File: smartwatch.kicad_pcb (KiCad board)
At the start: 4 copper layers, 38 x 38 mm, 52 parts, among them IC1 W25N01GVZEIG, IC2 NORA-B120-00B, J1 Charging_Pad-, J2 Charging_Pad+, J3 DS1020-09-15VBT1A, J4 Conn_01x04_Pin, Q1 2N7002, Q2 AO3401, Q6 AO3401, U1 MAX17048G+T10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

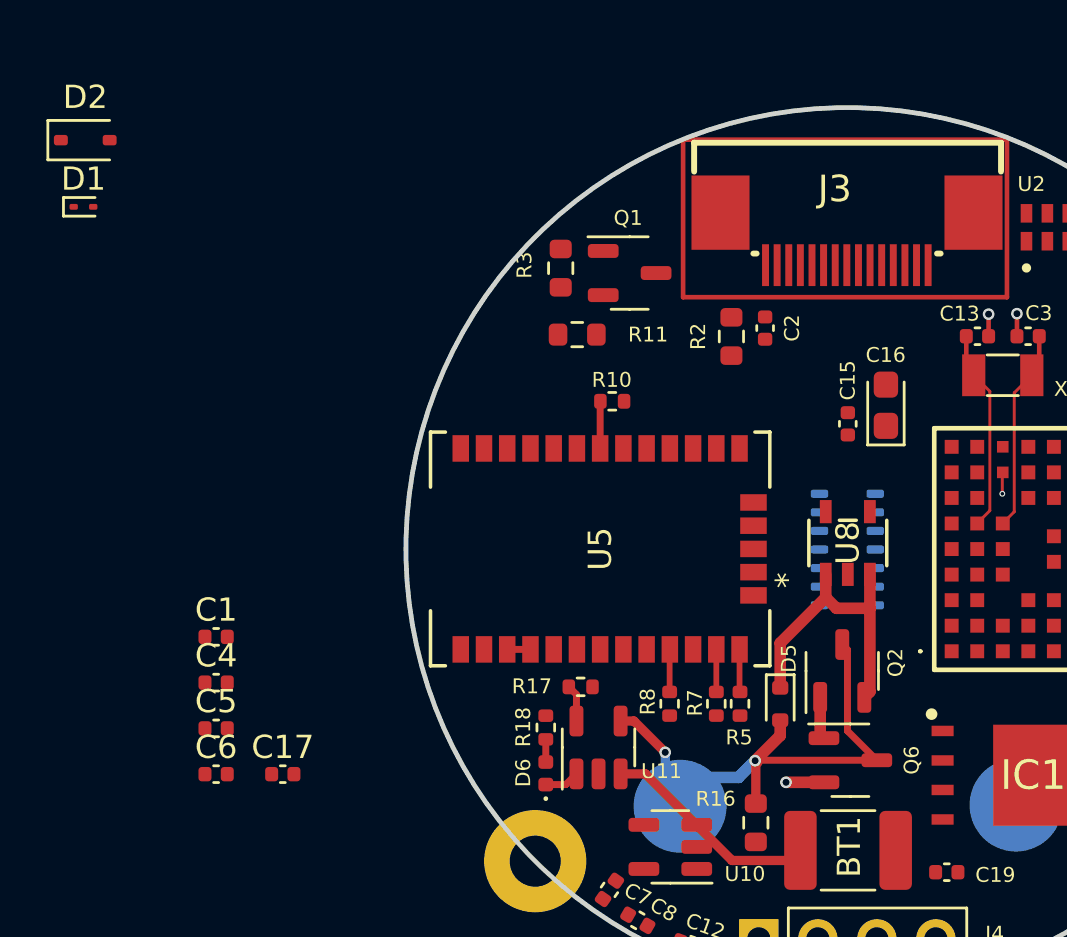
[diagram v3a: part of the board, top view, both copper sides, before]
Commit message: added lm66200
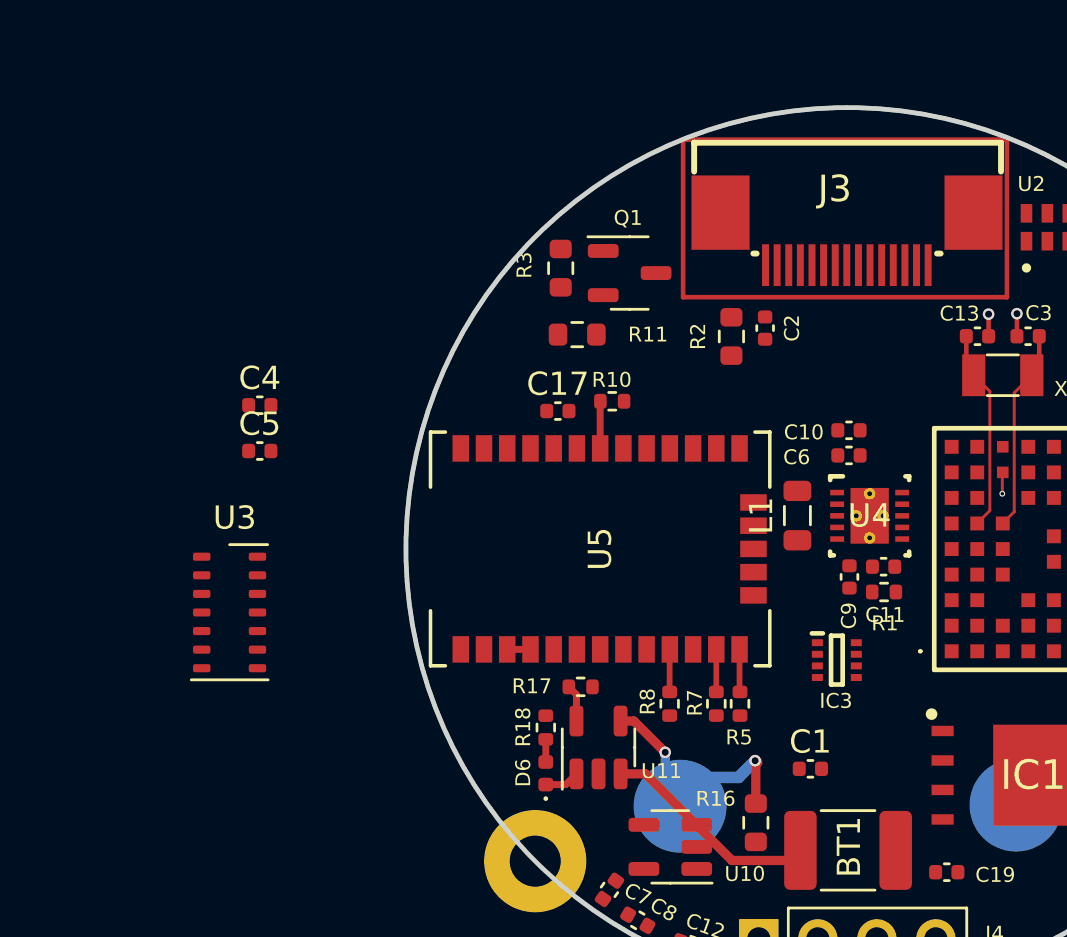
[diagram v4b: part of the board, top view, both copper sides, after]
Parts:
- removed C15: 100uF, Capacitor_SMD:C_0402_1005Metric
- removed C16: 4.7uF, Capacitor_Tantalum_SMD:CP_EIA-2012-12_Kemet-R
- removed D1: CDBQC0130L-HF, Diode_SMD:D_SOD-923
- removed D2: CUS08F30,H3F, Diode_SMD:D_SOD-323
- removed D5: LBAT54XV2T1G, Diode_SMD:D_SOD-523
- removed Q2, Q6: AO3401, Package_TO_SOT_SMD:SOT-23-3
- removed U8: AP2112K-3.3TRG1, AP2112K-3-3TRG1:SOT_RG1_DIO
- added C10: 10uF, Capacitor_SMD:C_0402_1005Metric, F.Cu at (152.6, 88.5)
- added C11: 0.1uF, Capacitor_SMD:C_0402_1005Metric, F.Cu at (154.1, 94.4)
- added C9: 10uF, Capacitor_SMD:C_0402_1005Metric, F.Cu at (152.6, 94.8)
- added IC3: LM66200DRLR, LM66200DRLR:SOTFL50P160X60-8N, F.Cu at (152.1, 98.4)
- added L1: MLZ2012M1R0HT000, Inductor_SMD:L_0805_2012Metric, F.Cu at (150.4, 92.2)
- added R1: 100, Resistor_SMD:R_0402_1005Metric, F.Cu at (154.1, 95.5)
- added U4: TPS63001DRCR, TPS63001DRCR:DRC0010J, F.Cu at (153.5, 92.2)
- C6: value 1uF -> 10uF
- U3: moved to F.Cu
- moved C6 30.5 mm to (152.6, 89.6)
- moved U3 26.7 mm to (125.9, 96.4), turned to 0 degrees
- moved C1 26.2 mm to (150.9, 103.1)
- moved C17 19.6 mm to (140.1, 87.7)
- moved C4 12.1 mm to (127.2, 87.5)
- moved C5 12.1 mm to (127.2, 89.4)
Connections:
- C1 pad 1: VBUS -> Net-(IC3-VIN1)
- C6 pad 1: Net-(D5-K) -> VSYS
- J2 pad 1: VBUS -> Net-(IC3-VIN1)
- R18 pad 1: VBUS -> Net-(IC3-VIN1)
- U10 pad 1: /BAT+ -> VBUS
- U10 pad 3: /BAT+ -> VBUS
- U11 pad 4: VBUS -> Net-(IC3-VIN1)
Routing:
- net Net-(D5-K): track 13.2 -> 0.00 mm
- net VBUS: track 24.1 -> 11.1 mm
- net Net-(Q2-D): track 1.82 -> 0.00 mm
- net /BAT+: track 11.6 -> 10.0 mm, vias 1 -> 0

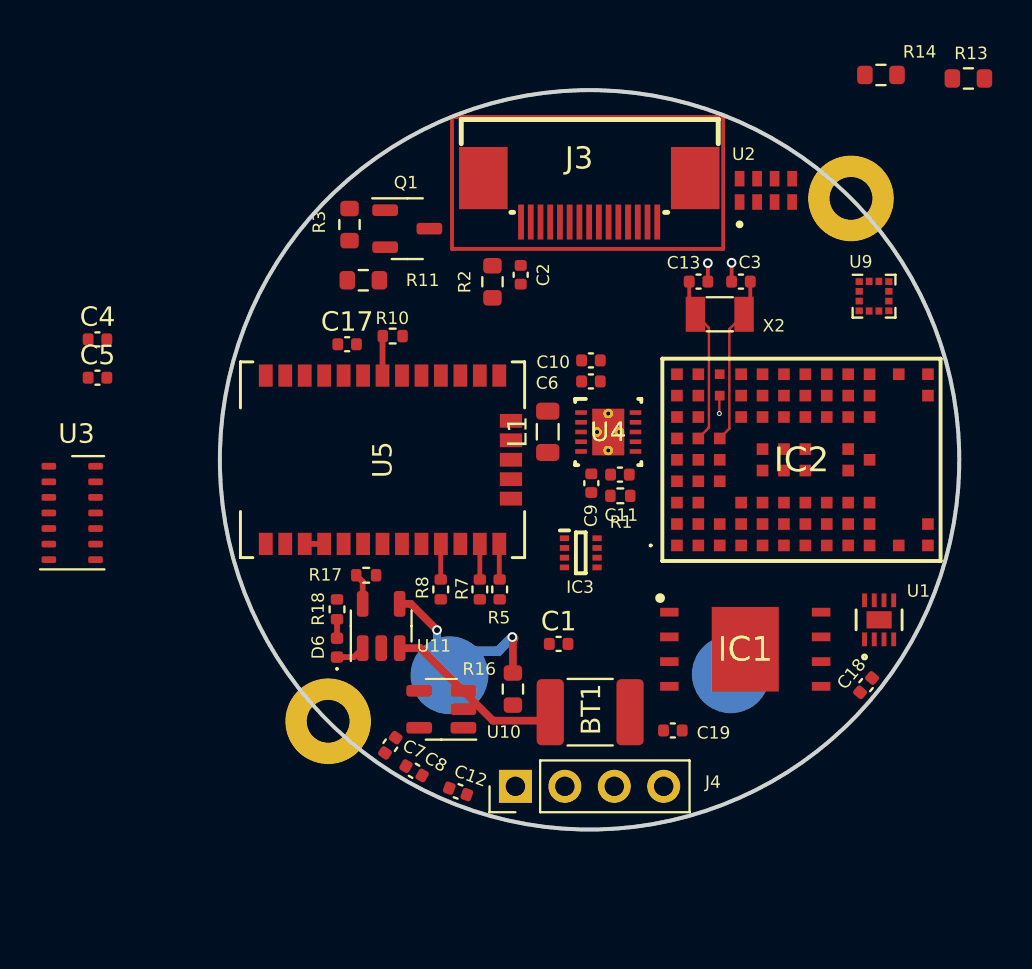
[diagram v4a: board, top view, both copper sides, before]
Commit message: signal routing 50% complete
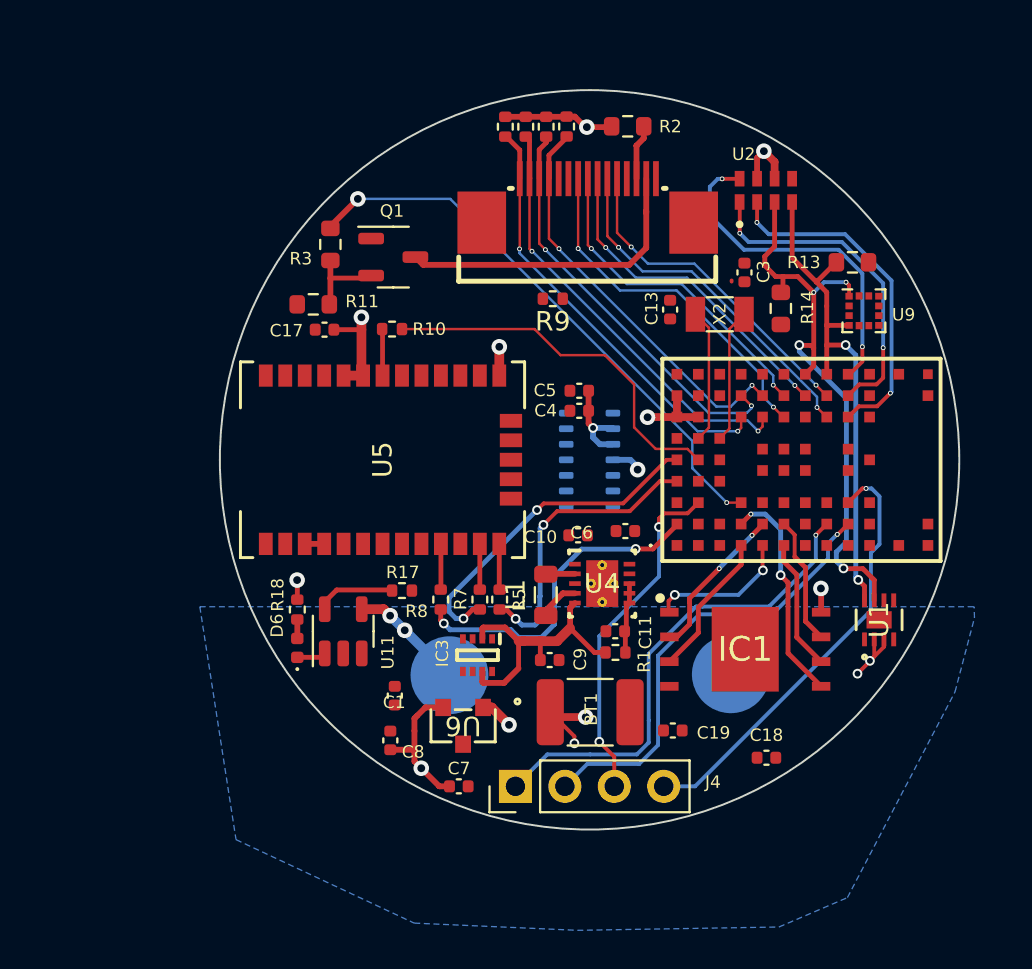
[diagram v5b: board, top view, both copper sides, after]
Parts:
- removed ? (x2): , 
- removed C12: 1uF, Capacitor_SMD:C_0402_1005Metric
- removed C2: 100uF, Capacitor_SMD:C_0402_1005Metric
- removed R16: 5.1k, Resistor_SMD:R_0603_1608Metric
- removed U10: AP2127K-1.8, Package_TO_SOT_SMD:SOT-23-5
- added R12: 4.7k, Resistor_SMD:R_0402_1005Metric, F.Cu at (151.3, 76.5)
- added R15: 4.7k, Resistor_SMD:R_0402_1005Metric, F.Cu at (149.2, 76.5)
- added R4: 4.7k, Resistor_SMD:R_0402_1005Metric, F.Cu at (148.2, 76.5)
- added R6: 4.7k, Resistor_SMD:R_0402_1005Metric, F.Cu at (150.3, 76.5)
- added R9: 4.7k, Resistor_SMD:R_0402_1005Metric, F.Cu at (150.6, 85.4)
- added U6: AP7313-18SAG-7, AP7313-18SAG-7:SOT-23_DIO, F.Cu at (146.0, 107.3)
- U11: value MCP73831-2-OT -> MCP73831T-2ACI/OT
- U3: moved to B.Cu
- moved U3 26.7 mm to (152.5, 93.6)
- moved C4 25.0 mm to (152.0, 91.1), turned to 180 degrees
- moved C5 24.8 mm to (152.0, 90.1), turned to 180 degrees
- moved R14 13.1 mm to (162.3, 85.9), turned to -90 degrees
- moved R13 11.2 mm to (166.0, 83.5), turned to 0 degrees
- moved R2 10.6 mm to (154.5, 76.5), turned to 0 degrees
- moved C9 9.34 mm to (150.5, 103.9), turned to 0 degrees
- moved C10 9.01 mm to (151.9, 97.5)
- moved C1 8.83 mm to (142.5, 105.8), turned to -90 degrees
- moved L1 8.38 mm to (150.3, 100.6)
- moved R1 8.05 mm to (153.8, 103.5)
- moved C11 8.05 mm to (153.8, 102.5)
- moved C6 7.89 mm to (154.3, 97.3)
- moved U4 7.80 mm to (153.2, 100.0)
- moved IC3 7.47 mm to (146.8, 103.7), turned to -90 degrees
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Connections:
- net Net-(U10-VOUT) renamed +1V8
- net VSYS renamed +3.3V
- IC2 pad A2: unconnected-(IC2-P0.12/TRACECLK/DCX-PadA2) -> /GPS_RESET
- IC2 pad A3: unconnected-(IC2-P1.03/TWI-PadA3) -> /TP_SDA
- IC2 pad A4: unconnected-(IC2-P1.00-PadA4) -> /GPS_TX
- IC2 pad A5: unconnected-(IC2-P0.20-PadA5) -> /GPS_RX
- IC2 pad B4: unconnected-(IC2-P1.02/TWI-PadB4) -> /TP_SCL
- IC2 pad B5: unconnected-(IC2-P0.03/NFC2-PadB5) -> /GPS_EXTINT
- IC2 pad C8: /RTC_CLK -> unconnected-(IC2-P0.22-PadC8)
- IC2 pad D3: unconnected-(IC2-P0.07/AIN3-PadD3) -> /BACKLIGHT_EN
- IC2 pad D7: /RTC_EVI -> /TP_SCL
- IC2 pad D8: unconnected-(IC2-P0.04/AIN0-PadD8) -> /TP_INT
- IC2 pad E7: unconnected-(IC2-P0.06/AIN2-PadE7) -> /TP_SDA
- IC2 pad E8: /BACKLIGHT_EN -> /TP_RST
- IC2 pad F7: /RTC_INT -> /DISPLAY_RESET
- IC2 pad F8: unconnected-(IC2-P1.14-PadF8) -> /DISPLAY_SDI
- IC2 pad G8: unconnected-(IC2-P1.12-PadG8) -> /DISPLAY_CLK
- IC2 pad H7: unconnected-(IC2-P0.29-PadH7) -> /DISPLAY_CS
- IC2 pad H8: unconnected-(IC2-P0.30-PadH8) -> /DISPLAY_D/C
- IC2 pad J7: unconnected-(IC2-P1.10-PadJ7) -> /RTC_INT
- IC2 pad J8: unconnected-(IC2-P0.28/AIN7-PadJ8) -> /RTC_CLK
- IC2 pad J9: unconnected-(IC2-P0.31-PadJ9) -> /RTC_EVI
- IC3 pad 4: unconnected-(IC3-~{ON}-Pad4) -> GND
- J3 pad 4: unconnected-(J3-Pad4) -> GND
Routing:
- net +3.3V: track 0.00 -> 82.4 mm, vias 0 -> 6
- net /BAT+: track 10.0 -> 73.4 mm, vias 0 -> 5
- net +1V8: track 0.00 -> 31.7 mm, vias 0 -> 2
- net /SCL: track 0.00 -> 31.0 mm, vias 0 -> 4
- net /BACKLIGHT_EN: track 0.00 -> 29.1 mm, vias 0 -> 2
- net /SDA: track 0.00 -> 26.7 mm, vias 0 -> 2
- net /SWDIO: track 0.00 -> 25.0 mm, vias 0 -> 1
- net /SWDCLK: track 0.00 -> 23.3 mm, vias 0 -> 1
- net /RESET_N: track 0.00 -> 22.5 mm, vias 0 -> 1
- net /TP_SDA: track 0.00 -> 22.3 mm, vias 0 -> 2
- net /TP_SCL: track 0.00 -> 22.1 mm, vias 0 -> 2
- net /TP_INT: track 0.00 -> 21.1 mm, vias 0 -> 2
- net /TP_RST: track 0.00 -> 20.9 mm, vias 0 -> 2
- net /DISPLAY_CLK: track 0.00 -> 20.7 mm, vias 0 -> 2
- net /GPS_EXTINT: track 0.00 -> 19.3 mm
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- added copper zone on B.Cu, net GND

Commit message: ready for production
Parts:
- removed C13, C3: 12pF, Capacitor_SMD:C_0402_1005Metric
- added R16: 4.7k, Resistor_SMD:R_0402_1005Metric, F.Cu at (155.3, 102.9)
- added R19: 4.7k, Resistor_SMD:R_0402_1005Metric, F.Cu at (168.8, 86.4)
- added R20: 4.7k, Resistor_SMD:R_0402_1005Metric, F.Cu at (159.0, 107.3)
- added R21: 4.7k, Resistor_SMD:R_0402_1005Metric, F.Cu at (163.9, 107.2)
- added REF**: MountingHole_2.2mm_M2, MountingHole:MountingHole_2.2mm_M2, F.Cu at (139.1, 107.1)
- added REF**: MountingHole_2.2mm_M2, MountingHole:MountingHole_2.2mm_M2, F.Cu at (165.9, 80.2)
- moved C19 7.74 mm to (149.1, 107.6), turned to -90 degrees
- moved C18 6.14 mm to (165.9, 104.5), turned to 90 degrees
- moved R9 4.55 mm to (150.1, 89.9), turned to 90 degrees
- moved C10 0.42 mm to (152.2, 97.2), turned to 180 degrees
- moved U6 0.31 mm to (145.8, 107.5)
- moved R13 0.30 mm to (166.3, 83.5)
- moved C6 0.28 mm to (154.1, 97.2)
- moved C7 0.19 mm to (145.9, 110.2)
- moved C1 0.08 mm to (142.5, 105.7)
- turned X2 to 180 degrees
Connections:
- IC2 pad A3: /TP_SDA -> unconnected-(IC2-P1.03/TWI-PadA3)
- IC2 pad B4: /TP_SCL -> unconnected-(IC2-P1.02/TWI-PadB4)
- J3 pad 4: GND -> +3.3V
- U4 pad V: (no net) -> GND
- X2 pad 1: /XL1 -> /XL2
- X2 pad 2: /XL2 -> /XL1
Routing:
- net +3.3V: track 82.4 -> 142.4 mm, vias 6 -> 14
- net /SDA: track 26.7 -> 48.8 mm, vias 2 -> 5
- net /SCL: track 31.0 -> 51.8 mm, vias 4 -> 5
- net /HR_INT: track 0.00 -> 6.43 mm, vias 0 -> 1
- net Net-(IC3-VIN1): track 14.2 -> 20.5 mm, vias 3 -> 5
- net GND: track 0.00 -> 6.11 mm, vias 0 -> 75
- net /FLASH_IO3: track 6.59 -> 12.0 mm
- net VBUS: track 16.2 -> 21.5 mm, vias 1 -> 2
- net /FLASH_IO2: track 7.50 -> 12.0 mm
- net /DISPLAY_CLK: track 20.7 -> 17.1 mm
- net /BAT+: track 73.4 -> 76.0 mm, vias 5 -> 4
- net /FLASH_CS: track 7.38 -> 9.34 mm
- net +1V8: track 31.7 -> 29.9 mm
- net /GPS_RX: track 17.3 -> 15.8 mm
- net /RTC_INT: track 17.7 -> 18.9 mm, vias 2 -> 3
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- added copper zone on F.Cu, net GND
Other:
- board text added: "+"
- board text added: "-"
- board text added: "Designed by Iiro Karppanen"

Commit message: update 1
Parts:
- removed C11: 0.1uF, Capacitor_SMD:C_0402_1005Metric
- removed L1: MLZ2012M1R0HT000, Inductor_SMD:L_0805_2012Metric
- removed R1: 100, Resistor_SMD:R_0402_1005Metric
- added C2: 0.1uF, Capacitor_SMD:C_0402_1005Metric, F.Cu at (152.2, 104.1)
- added L2: MAMK2520H1R5M, Inductor_SMD:L_1008_2520Metric, F.Cu at (151.8, 98.3)
- U4: value TPS63001DRCR -> TPS63031DSK; footprint TPS63001DRCR:DRC0010J -> Package_SON:WSON-10-1EP_2.5x2.5mm_P0.5mm_EP1.2x2mm
- moved C6 4.02 mm to (155.3, 101.0), turned to -90 degrees
- moved C9 3.26 mm to (149.5, 100.8), turned to 90 degrees
- moved C10 2.76 mm to (154.5, 98.6), turned to 90 degrees
- moved U4 1.86 mm to (152.2, 101.6), turned to -90 degrees
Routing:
- net VBUS: track 21.5 -> 17.8 mm
- net /GPS_TX: track 15.6 -> 13.6 mm
- net /SWDIO: track 25.0 -> 24.0 mm
- net /SWDCLK: track 23.3 -> 22.4 mm
- net +3.3V: track 142.4 -> 143.2 mm, vias 14 -> 13
- net Net-(U4-EN): track 3.66 -> 2.88 mm
- net Net-(U4-L2): track 1.51 -> 2.14 mm
- net GND: vias 75 -> 71
